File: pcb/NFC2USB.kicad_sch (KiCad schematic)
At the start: 13 parts, among them J1 USB_C_USB2.0, SW2 MODE, U1 NFCModuleRC522, U2 AMS1117-3.3

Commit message: style: update Titles
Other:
- title: NFC2USB -> Bloop NFC Scanner
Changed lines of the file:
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@@
   (paper "A4")
   (title_block
-    (title "NFC2USB")
+    (title "Bloop NFC Scanner")
     (date "${DATE}")
     (rev "${VERSION}")

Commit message: feat: switch LED colors
Switching the Activity and Ready LEDs for visibility reasons
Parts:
- D1: LCSC C72043 -> C72038
- D2: LCSC C72038 -> C72043
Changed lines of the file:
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@@
       (effects (font (size 1.27 1.27)) hide)
     )
-    (property "LCSC" "C72038" (id 4) (at 172.72 95.25 0)
+    (property "LCSC" "C72043" (id 4) (at 172.72 95.25 0)
       (effects (font (size 1.27 1.27)) hide)
     )
@@
       (effects (font (size 1.27 1.27)) hide)
     )
-    (property "LCSC" "C72043" (id 4) (at 180.34 95.25 0)
+    (property "LCSC" "C72038" (id 4) (at 180.34 95.25 0)
       (effects (font (size 1.27 1.27)) hide)
     )

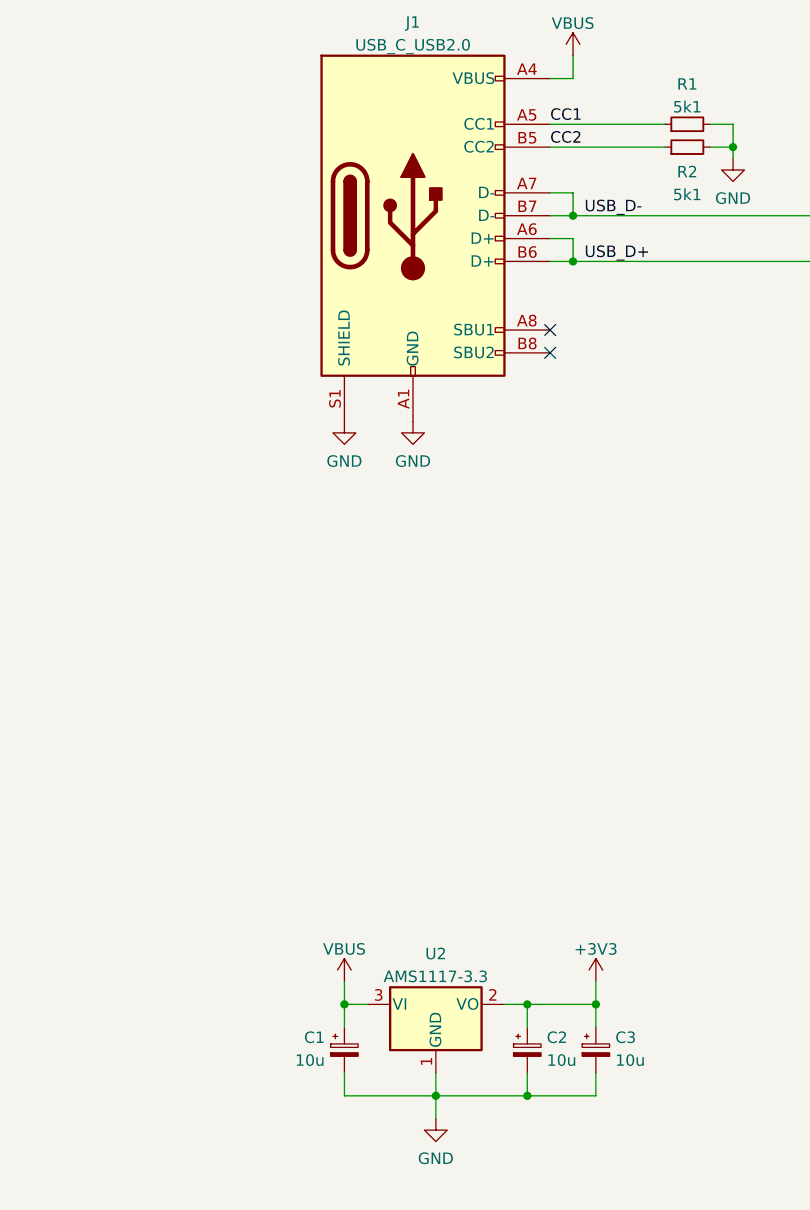
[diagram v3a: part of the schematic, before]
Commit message: fix: change mouse bites position, add silkscreen
This commit includes the switch to KiCad 7 which is why there are so many unrelated changes in the files
The mousebites were moved away from the mode switch
Silkscreen text was added for mode switch and LEDs
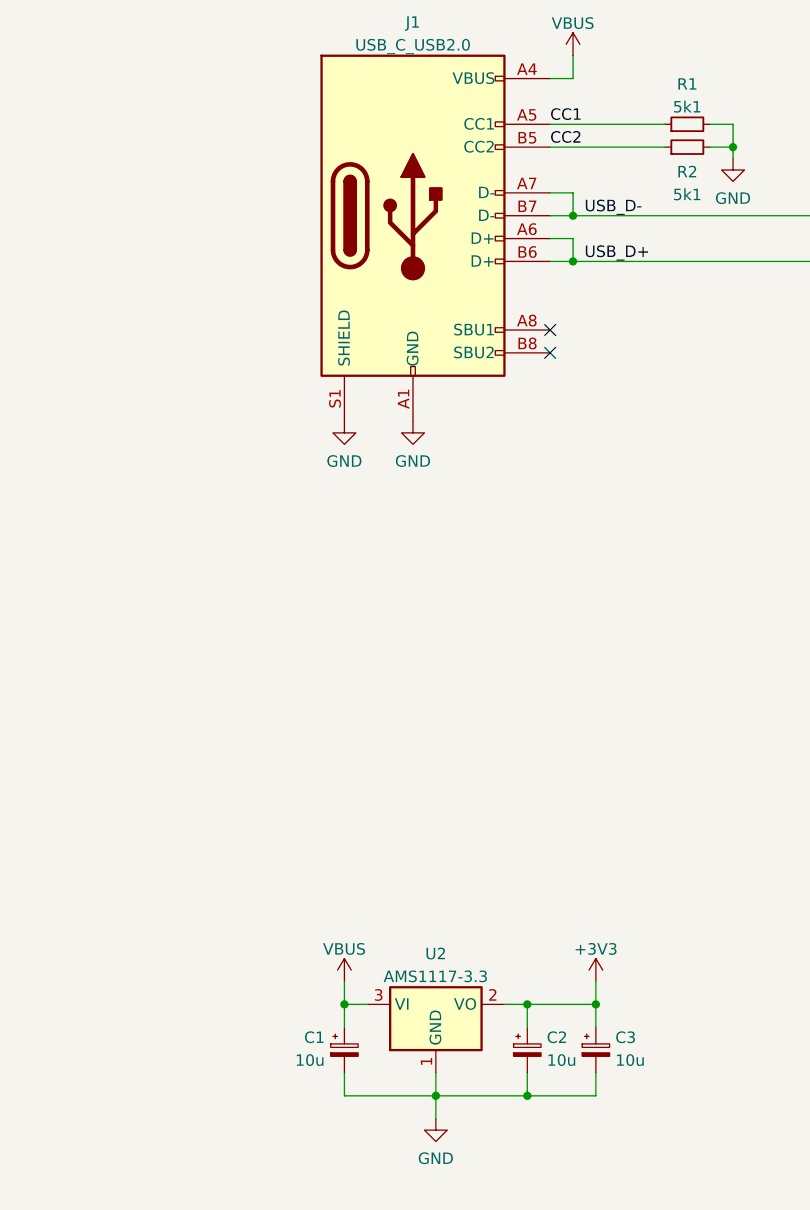
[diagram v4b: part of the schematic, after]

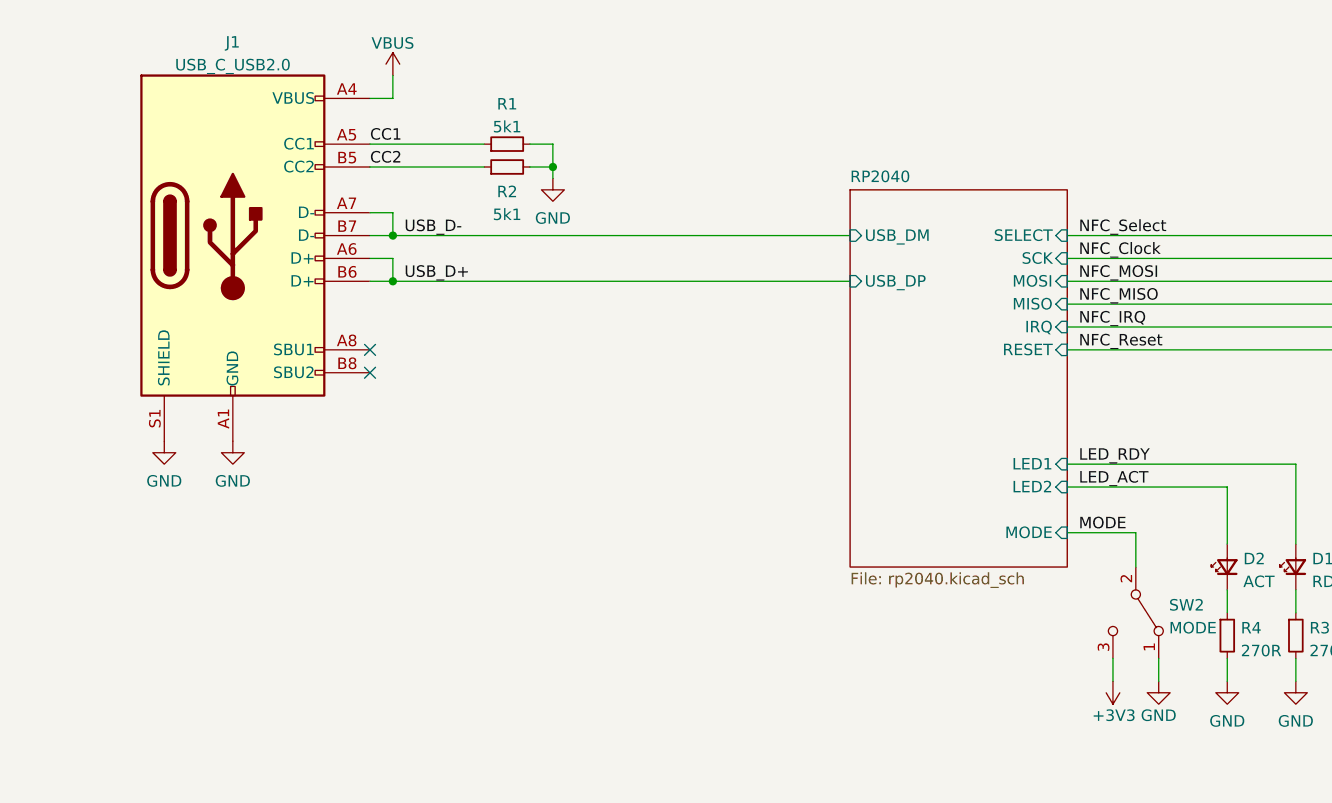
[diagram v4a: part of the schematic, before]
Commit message: chore: update to KiCad 8
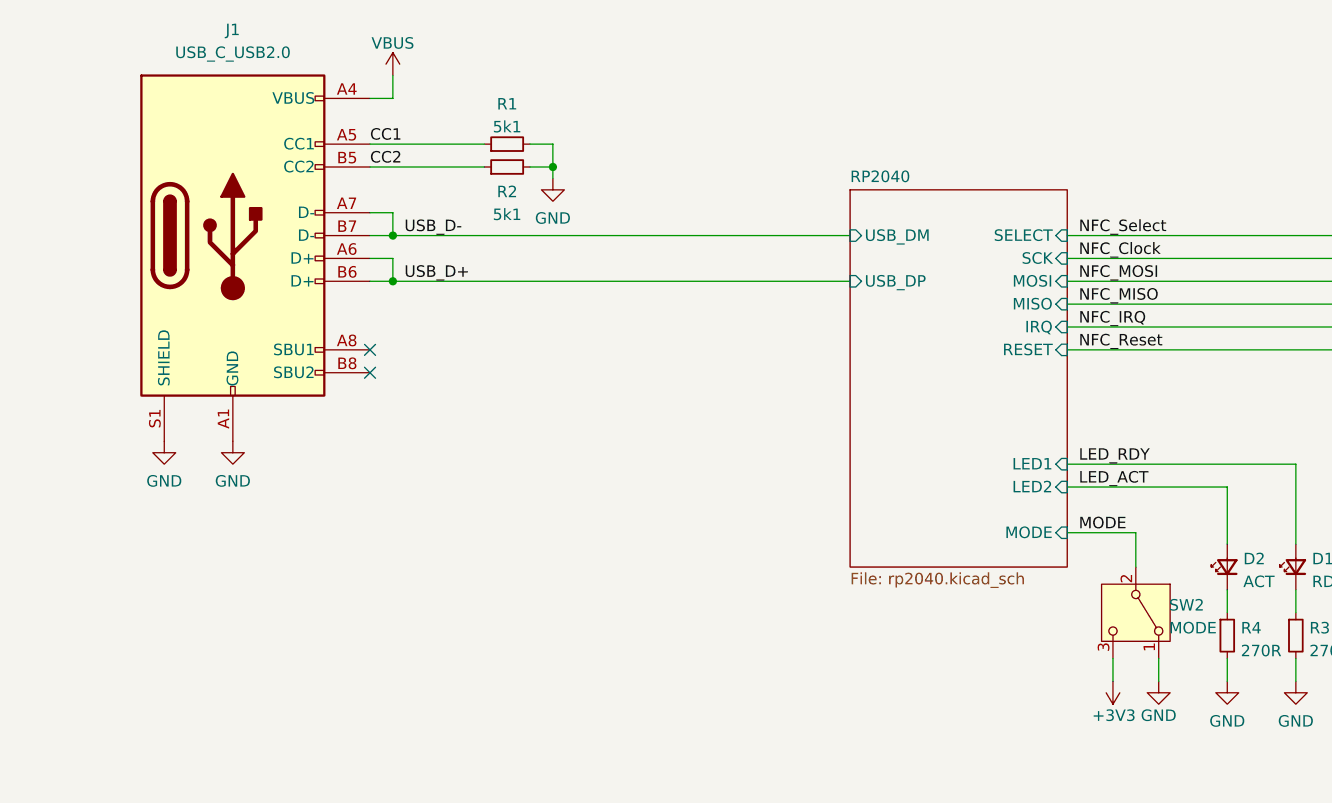
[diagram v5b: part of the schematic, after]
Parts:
- J1: symbol Connector:USB_C_Receptacle_USB2.0 -> Connector:USB_C_Receptacle_USB2.0_16P

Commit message: fix: add part number for connector
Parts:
- U1: LCSC (none) -> C2897390
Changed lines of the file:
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@@
+			)
+		)
+		(property "LCSC" "C2897390"
+			(at 219.71 49.53 0)
+			(effects
+				(font
+					(size 1.27 1.27)
+				)
+				(hide yes)
 			)
 		)
